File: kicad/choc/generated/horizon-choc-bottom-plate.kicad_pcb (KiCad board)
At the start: 2 copper layers, 252 x 68 mm, 114 parts

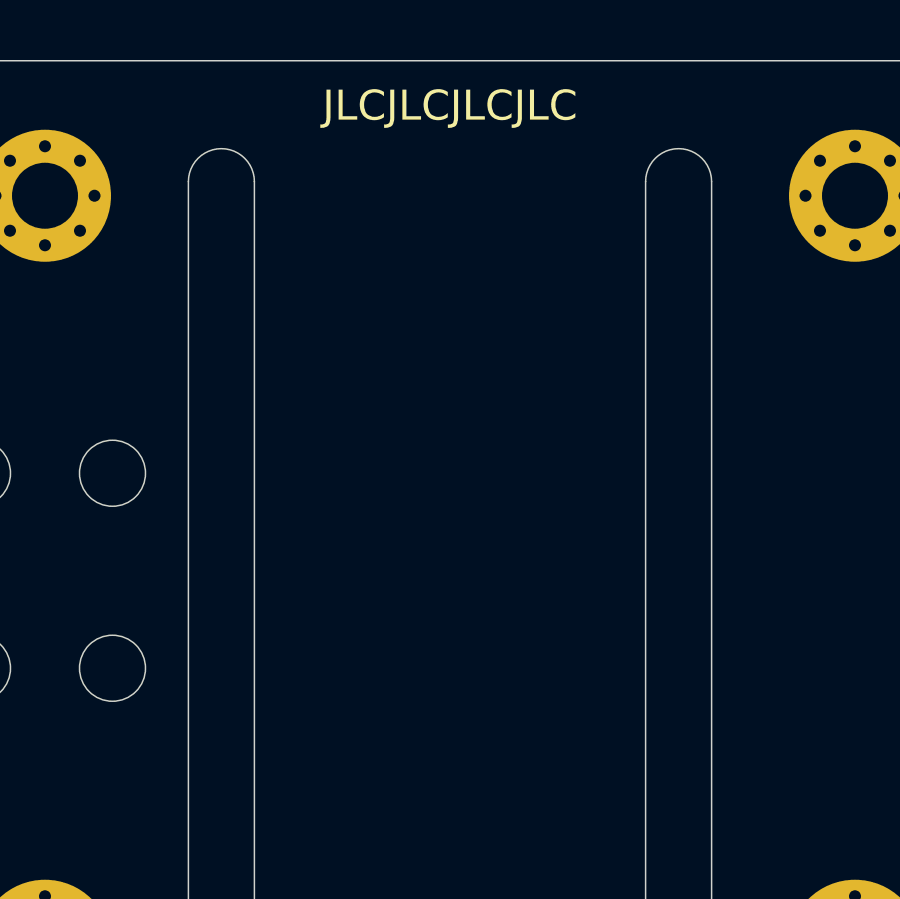
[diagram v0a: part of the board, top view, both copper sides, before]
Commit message: Preserve logos on plate PCBs
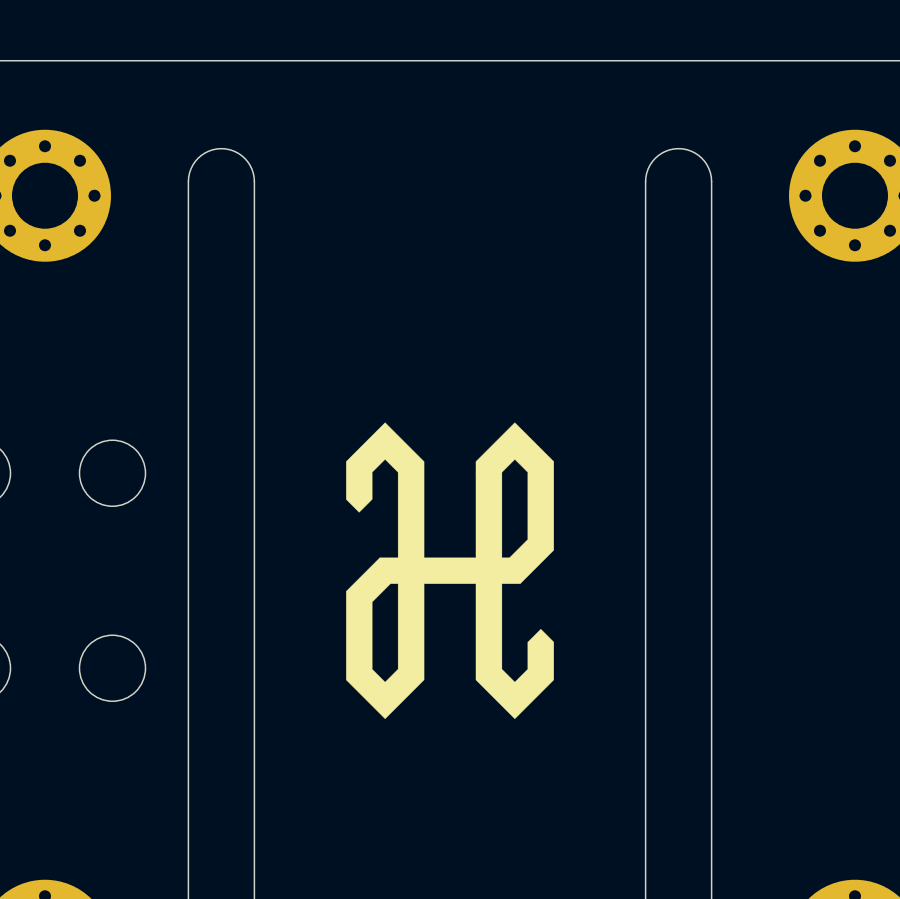
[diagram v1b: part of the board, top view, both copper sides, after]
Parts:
- added ?: Logo-Top, horizon-footprints:Logo_Horizon_H, F.Cu at (202.0, 112.0)
- added ?: Logo-Bottom, horizon-footprints:Logo_Horizon_Small, B.Cu at (202.0, 100.5)
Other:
- board text added: "github.com/skarrmann/horizon"
- board text added: "rev2 | Choc"

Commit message: Remove unused footprints and other files. Update readme. Prepare for production!
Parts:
- moved ? 11.0 mm to (202.0, 111.5)
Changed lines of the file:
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@@
   )
   (module horizon-footprints:Logo_Horizon_Small (layer B.Cu)
-    (at 202 100.5 180)
+    (at 202 111.5 180)
     (fp_text reference "" (at 0 -2) (layer B.SilkS) hide
       (effects (font (size 1.524 1.524) (thickness 0.3)) (justify mirror))
@@
   (gr_line (start 328 161) (end 328 97) (layer Edge.Cuts) (width 0.05))
   (gr_line (start 78 163) (end 326 163) (layer Edge.Cuts) (width 0.05))
-  (gr_text "rev2 | Choc" (at 202 104.5) (layer B.SilkS)
+  (gr_text "rev2 | Choc" (at 202 115.5) (layer B.SilkS)
     (effects (font (size 1 1) (thickness 0.15)) (justify mirror))
   )
-  (gr_text JLCJLCJLCJLC (at 202 106.5) (layer B.SilkS)
+  (gr_text JLCJLCJLCJLC (at 202 127.5) (layer B.SilkS)
     (effects (font (size 1 1) (thickness 0.15)) (justify mirror))
   )
